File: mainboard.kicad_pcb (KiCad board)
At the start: 2 copper layers, 88 x 100 mm, 57 parts, among them J1 USB_C_Receptacle_USB2.0, J2 GPIO, J3 RJ45, J4 RJ45, J5 Conn_01x02_Socket, J6 Conn_01x03_Socket, M1 Fan, Q1 MMBT3904, Q2 MMBT3906, Q3 SSM3J332R, Q4 MMBT3906, SW1 SW_DIP_x02, U1 CH221K, U2 MCP251863, U3 NJM2845DL1, U4 MSP2807, U5 IM920c_ADP_IM920conn, Y1 4MHz

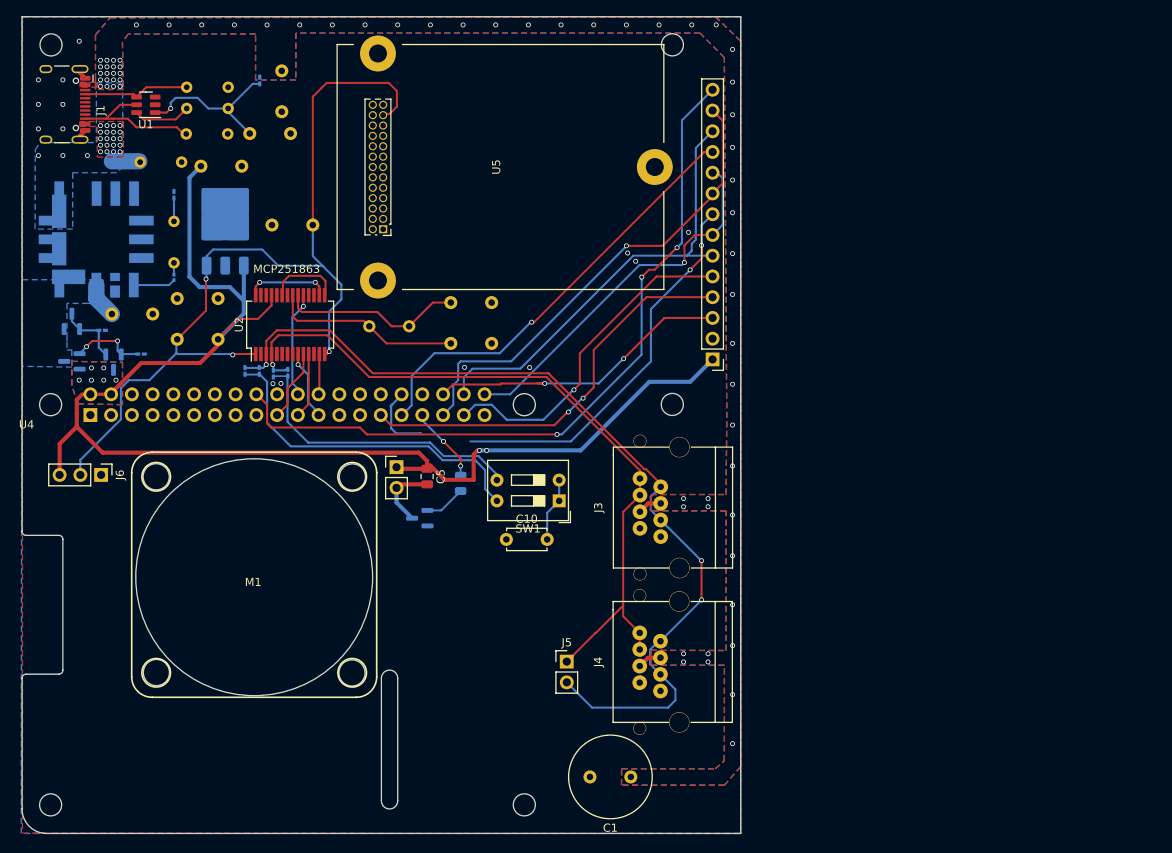
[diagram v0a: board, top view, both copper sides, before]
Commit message: チップ抵抗に変更
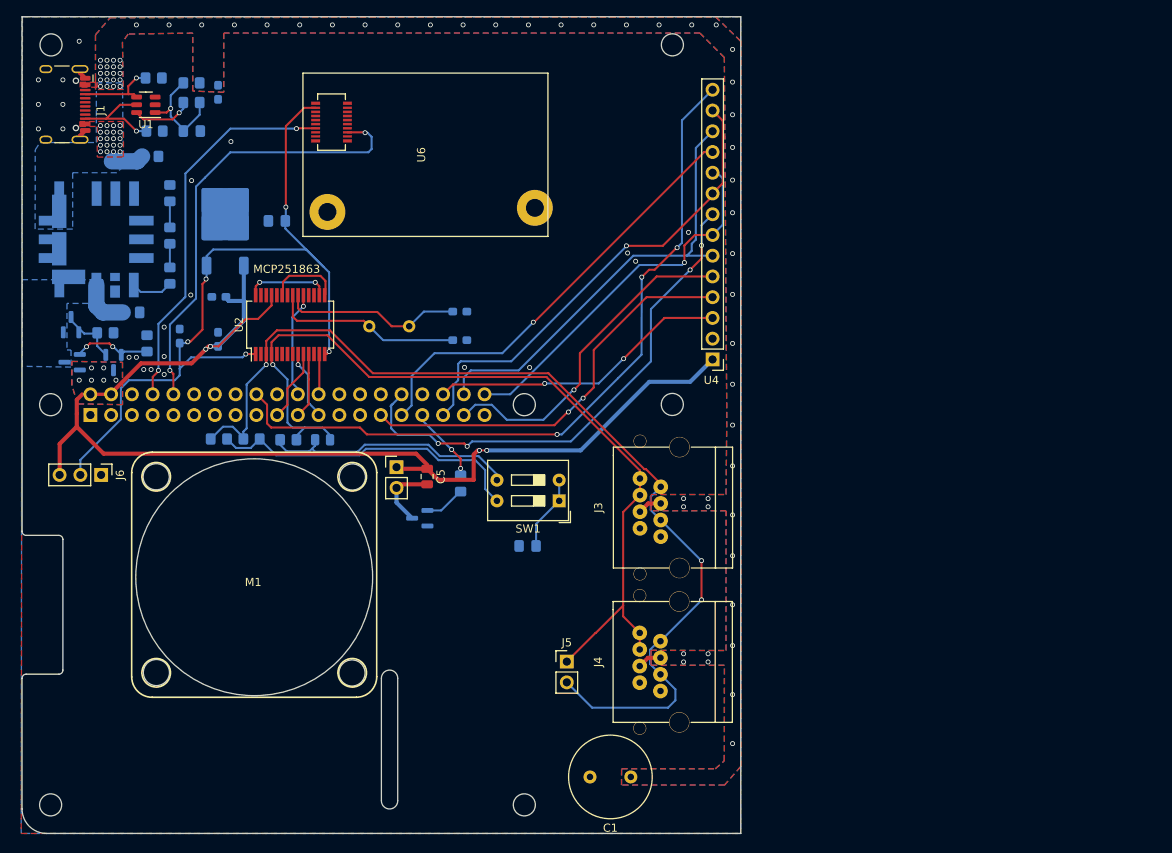
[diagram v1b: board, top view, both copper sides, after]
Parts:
- removed U5: IM920c_ADP_IM920conn, interplan:IM920(IM920c_ADP)
- added U6: IM920sl, interplan:IM920s, F.Cu at (157.5, 70.8)
- C10: footprint Capacitor_THT:C_Disc_D4.7mm_W2.5mm_P5.00mm -> Capacitor_SMD:C_0805_2012Metric_Pad1.18x1.45mm_HandSolder; moved to B.Cu
- C11: value 0.33μF -> 0.1μF; footprint Capacitor_THT:C_Disc_D4.7mm_W2.5mm_P5.00mm -> Capacitor_SMD:C_0603_1608Metric_Pad1.08x0.95mm_HandSolder
- C12: value 2.2µF -> 10µF; footprint Capacitor_THT:C_Disc_D4.7mm_W2.5mm_P5.00mm -> Capacitor_SMD:C_0805_2012Metric_Pad1.18x1.45mm_HandSolder
- C2, C4: footprint Capacitor_THT:C_Disc_D4.7mm_W2.5mm_P5.00mm -> Capacitor_SMD:C_0805_2012Metric_Pad1.18x1.45mm_HandSolder
- C3, C6, C7, C8, C9: footprint Capacitor_THT:C_Disc_D4.7mm_W2.5mm_P5.00mm -> Capacitor_SMD:C_0603_1608Metric_Pad1.08x0.95mm_HandSolder
- R1, R10, R11, R12, R13, R14, R9: footprint Resistor_SMD:R_0201_0603Metric_Pad0.64x0.40mm_HandSolder -> Resistor_SMD:R_0805_2012Metric_Pad1.20x1.40mm_HandSolder
- R15: footprint Resistor_SMD:R_0201_0603Metric_Pad0.64x0.40mm_HandSolder -> Resistor_SMD:R_0805_2012Metric
- R2, R3, R4, R5, R8: footprint Resistor_THT:R_Axial_DIN0204_L3.6mm_D1.6mm_P5.08mm_Horizontal -> Resistor_SMD:R_0805_2012Metric_Pad1.20x1.40mm_HandSolder
- R6: footprint Diode_SMD:D_0805_2012Metric -> Resistor_SMD:R_0805_2012Metric_Pad1.20x1.40mm_HandSolder
- R7: footprint Resistor_SMD:R_0201_0603Metric -> Resistor_SMD:R_0805_2012Metric_Pad1.20x1.40mm_HandSolder
- U3: value NJM2845DL1 -> NJM2391; footprint Package_TO_SOT_SMD:TO-252-3_TabPin2 -> Package_TO_SOT_SMD:TO-252-2
- moved C11 16.2 mm to (132.2, 88.2), turned to 180 degrees
- moved R15 9.24 mm to (144.9, 105.7), turned to 0 degrees
- moved R12 8.93 mm to (132.2, 105.5), turned to 180 degrees
- moved R13 8.39 mm to (136.2, 105.5), turned to 180 degrees
- moved R1 8.36 mm to (128.9, 62.0), turned to 180 degrees
- moved R14 8.30 mm to (140.8, 105.7), turned to 0 degrees
- moved C3 8.23 mm to (132.2, 63.1)
- moved C2 7.10 mm to (128.9, 67.8)
- moved R4 4.55 mm to (128.9, 64.3)
- moved C12 4.43 mm to (139.3, 78.8)
- moved R2 4.20 mm to (124.3, 61.4)
- moved C9 4.05 mm to (161.8, 90.0)
- moved C8 3.92 mm to (161.8, 93.5)
- moved R3 3.89 mm to (124.4, 67.8)
- moved R8 3.38 mm to (126.2, 80.7)
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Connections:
- J2 pad 10: /GPIO15/RXD0 -> UART RXD
- J2 pad 8: /GPIO14/TXD0 -> UART TXD
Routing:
- net UART RXD: track 0.00 -> 55.1 mm, vias 0 -> 2
- net UART TXD: track 0.00 -> 47.0 mm, vias 0 -> 2
- net +5V: track 165.6 -> 147.0 mm, vias 8 -> 10
- net /canfd/CANH: track 91.4 -> 105.0 mm
- net /canfd/CANL: track 111.1 -> 123.8 mm
- net +3.3V: track 109.5 -> 98.5 mm, vias 3 -> 5
- net Net-(U1-VDD): track 20.9 -> 13.3 mm
- net LED: track 56.3 -> 63.2 mm, vias 2 -> 4
- net Net-(J1-CC2): track 17.5 -> 12.2 mm, vias 0 -> 1
- net Net-(R14-Pad1): track 36.6 -> 31.6 mm
- net Net-(J1-CC1): track 13.1 -> 9.62 mm, vias 0 -> 1
- net Net-(R12-Pad1): track 41.5 -> 39.1 mm
- net Net-(P1-Sence): track 4.33 -> 6.10 mm
- net Net-(C10-Pad2): track 7.57 -> 9.24 mm
- net Net-(R7-Pad2): track 1.46 -> 2.90 mm
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
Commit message: first commit
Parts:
- removed ? (x3): , 
- removed C10: 4700pF, Capacitor_SMD:C_0805_2012Metric_Pad1.18x1.45mm_HandSolder
- removed C11: 0.1μF, Capacitor_SMD:C_0603_1608Metric_Pad1.08x0.95mm_HandSolder
- removed C12: 10µF, Capacitor_SMD:C_0805_2012Metric_Pad1.18x1.45mm_HandSolder
- removed M1: Fan, pihat_cooling:fan_30mm
- removed Q2, Q4: MMBT3906, Package_TO_SOT_SMD:SOT-23
- removed R10: 10KΩ, Resistor_SMD:R_0805_2012Metric_Pad1.20x1.40mm_HandSolder
- removed R12, R13, R14: 120Ω, Resistor_SMD:R_0805_2012Metric_Pad1.20x1.40mm_HandSolder
- removed R15: 120Ω, Resistor_SMD:R_0805_2012Metric
- removed S1, S2, S3, S4: M3, screw:M3
- removed SW1: SW_DIP_x02, Button_Switch_THT:SW_DIP_SPSTx02_Slide_9.78x7.26mm_W7.62mm_P2.54mm
- removed U6: IM920sl, interplan:IM920s
- removed Y1: 4MHz, Crystal:Crystal_HC49-U_Vertical
- added IC1: AZ1117CH-3.3TRG1, OKL:SOT230P700X180-4N, F.Cu at (130.2, 109.8)
- added J10: RJ45, OKL:7810-8P8C, F.Cu at (143.0, 145.0)
- added J11: Conn_01x02, Connector_JST:JST_XH_B2B-XH-A_1x02_P2.50mm_Vertical, F.Cu at (160.8, 150.8)
- added J13: Conn_01x04_Socket, Connector_JST:JST_XH_B4B-XH-A_1x04_P2.50mm_Vertical, F.Cu at (132.2, 133.1)
- added J2: Conn_01x03_Socket, Connector_PinHeader_2.54mm:PinHeader_1x03_P2.54mm_Vertical, F.Cu at (150.7, 110.1)
- added J7: Conn_01x04, Connector_JST:JST_XH_B4B-XH-A_1x04_P2.50mm_Vertical, F.Cu at (170.0, 136.0)
- added J8: Conn_01x02, Connector_JST:JST_XH_B2B-XH-A_1x02_P2.50mm_Vertical, F.Cu at (160.8, 142.9)
- added J9: RJ45, OKL:7810-8P8C, F.Cu at (123.0, 145.0)
- added X1: CSX-750P, OKL:CSX-750P, F.Cu at (144.4, 121.0)
- C1: value 1000μF -> 0.1μF; footprint Capacitor_THT:C_Radial_D10.0mm_H12.5mm_P5.00mm -> Capacitor_SMD:C_0603_1608Metric_Pad1.08x0.95mm_HandSolder
- C2: value 1μF -> 10µF; moved to F.Cu
- C3, C7: moved to F.Cu
- C4: value 10μF -> 0.1μF; footprint Capacitor_SMD:C_0805_2012Metric_Pad1.18x1.45mm_HandSolder -> Capacitor_SMD:C_0603_1608Metric_Pad1.08x0.95mm_HandSolder; moved to F.Cu
- C5: value 100nF -> 10μF; footprint Capacitor_SMD:C_0805_2012Metric -> Capacitor_SMD:C_0805_2012Metric_Pad1.18x1.45mm_HandSolder
- C6: value 0.1μF -> 100nF; footprint Capacitor_SMD:C_0603_1608Metric_Pad1.08x0.95mm_HandSolder -> Capacitor_SMD:C_0805_2012Metric; moved to F.Cu
- C8: value 22pF -> 0.1μF; moved to F.Cu
- C9: value 22pF -> 22μF; footprint Capacitor_SMD:C_0603_1608Metric_Pad1.08x0.95mm_HandSolder -> Capacitor_SMD:C_0805_2012Metric_Pad1.18x1.45mm_HandSolder; moved to F.Cu
- J1: value USB_C_Receptacle_USB2.0 -> Conn_01x04; footprint Connector_USB:USB_C_Receptacle_HCTL_HC-TYPE-C-16P-01A -> Connector_JST:JST_XH_B4B-XH-A_1x04_P2.50mm_Vertical
- J3: value RJ45 -> Conn_01x02_Socket; footprint akiRJ45:7810-8P8C -> Connector_PinHeader_2.54mm:PinHeader_1x02_P2.54mm_Vertical
- J4: value RJ45 -> Conn_01x04; footprint akiRJ45:7810-8P8C -> Connector_JST:JST_XH_B4B-XH-A_1x04_P2.50mm_Vertical
- J5: value Conn_01x02_Socket -> Conn_01x02; footprint Connector_PinHeader_2.54mm:PinHeader_1x02_P2.54mm_Vertical -> Connector_JST:JST_XH_B2B-XH-A_1x02_P2.50mm_Vertical
- J6: value Conn_01x03_Socket -> Conn_01x02; footprint Connector_PinHeader_2.54mm:PinHeader_1x03_P2.54mm_Vertical -> Connector_JST:JST_XH_B2B-XH-A_1x02_P2.50mm_Vertical
- P1: value ~ -> OKLT6W12NC; footprint okL:OKLT6W12NC -> OKL:OKLT6W12NC; moved to F.Cu
- Q1: value MMBT3904 -> IRFML8244TRPBF; footprint Package_TO_SOT_SMD:SOT-23 -> Package_TO_SOT_SMD:SOT-23-3; moved to F.Cu
- Q3: value SSM3J332R -> IRFML8244TRPBF; footprint Package_TO_SOT_SMD:SOT-23 -> Package_TO_SOT_SMD:SOT-23-3; moved to F.Cu
- R1: value 1kΩ -> 120Ω; moved to F.Cu
- R11: value 10KΩ -> R; footprint Resistor_SMD:R_0805_2012Metric_Pad1.20x1.40mm_HandSolder -> Resistor_SMD:R_0603_1608Metric_Pad0.98x0.95mm_HandSolder; moved to F.Cu
- R2: value 5.1kΩ -> 330Ω; moved to F.Cu
- R3: value 5.1kΩ -> 1kΩ; moved to F.Cu
- R4: value 47kΩ -> R; footprint Resistor_SMD:R_0805_2012Metric_Pad1.20x1.40mm_HandSolder -> Resistor_SMD:R_0603_1608Metric_Pad0.98x0.95mm_HandSolder; moved to F.Cu
- R5: value 20KΩ -> 10Ω; moved to F.Cu
- R6: value 100 -> R; footprint Resistor_SMD:R_0805_2012Metric_Pad1.20x1.40mm_HandSolder -> Resistor_SMD:R_0603_1608Metric_Pad0.98x0.95mm_HandSolder
- R7: value 1kΩ -> R; footprint Resistor_SMD:R_0805_2012Metric_Pad1.20x1.40mm_HandSolder -> Resistor_SMD:R_0603_1608Metric_Pad0.98x0.95mm_HandSolder
- R8: value 330Ω -> R; footprint Resistor_SMD:R_0805_2012Metric_Pad1.20x1.40mm_HandSolder -> Resistor_SMD:R_0603_1608Metric_Pad0.98x0.95mm_HandSolder
- R9: value 10Ω -> R; footprint Resistor_SMD:R_0805_2012Metric_Pad1.20x1.40mm_HandSolder -> Resistor_SMD:R_0603_1608Metric_Pad0.98x0.95mm_HandSolder; moved to F.Cu
- U1: value CH221K -> MCP251863; footprint Package_TO_SOT_SMD:SOT-23-6 -> Package_SO:SSOP-28_5.3x10.2mm_P0.65mm
- U2: value MCP251863 -> TCA9803; footprint Package_SO:SSOP-28_5.3x10.2mm_P0.65mm -> Package_SO:VSSOP-8_3.0x3.0mm_P0.65mm
- U3: value NJM2391 -> TCA9803; footprint Package_TO_SOT_SMD:TO-252-2 -> Package_SO:VSSOP-8_3.0x3.0mm_P0.65mm; moved to F.Cu
- U4: value MSP2807 -> TCA9803; footprint MSP2807:MSP2807 -> Package_SO:VSSOP-8_3.0x3.0mm_P0.65mm
- moved R8 75.3 mm to (155.4, 150.1), turned to -90 degrees
- moved J1 72.3 mm to (170.0, 108.0)
- moved R7 63.8 mm to (155.2, 142.4)
- moved C9 62.4 mm to (119.5, 135.8), turned to 0 degrees
- moved R4 60.1 mm to (153.8, 119.0)
- moved R1 57.6 mm to (154.7, 113.4), turned to 0 degrees
- moved P1 57.0 mm to (114.8, 131.8), turned to 90 degrees
- moved C3 55.9 mm to (161.6, 110.6), turned to 0 degrees
- moved R2 55.6 mm to (131.5, 116.5)
- moved U3 55.2 mm to (162.5, 126.0), turned to 0 degrees
- moved R9 52.4 mm to (131.4, 127.6)
- moved C1 52.1 mm to (149.6, 106.6), turned to 0 degrees
- moved U1 50.7 mm to (142.4, 111.6), turned to -90 degrees
- moved R5 49.7 mm to (132.6, 119.9), turned to -90 degrees
- moved R3 48.8 mm to (127.0, 116.6)
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- renumbered J2 to J12
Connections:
- net D/C renamed EN_3
- C1 pad 1: +12V -> +3.3V
- C2 pad 1: Net-(U1-VDD) -> +3.3V
- C3 pad 1: +12V -> +3.3V
- C4 pad 1: Net-(P1-Sence) -> +5V
- C5 pad 2: Net-(M1--) -> GND
- C7 pad 1: +5V -> +3.3V
- C8 pad 1: GND -> +3.3V
- C8 pad 2: Net-(U2-OSC1) -> GND
- C9 pad 1: GND -> +12V
- C9 pad 2: Net-(U2-OSC2) -> GND
- J12 pad 11: /GPIO17 -> LED_B
- J12 pad 13: /GPIO27 -> LED_R
- J12 pad 32: LED -> limit1
- J12 pad 33: GPIO13/PWM1 -> EN_1
- J12 pad 35: SPI1.MISO -> EN_2
- J12 pad 36: SPI1.CE0 -> limit2
- J12 pad 38: SPI1.MOSI -> limit3
- J12 pad 40: SPI1.SCLK -> limit4
- J3 pad 1: /canfd/CANH -> Net-(J3-Pin_1)
- J3 pad 2: /canfd/CANL -> /canfd/CANH
- J4 pad 1: /canfd/CANH -> Net-(J4-Pin_1)
- J4 pad 2: /canfd/CANL -> Net-(J4-Pin_2)
- J4 pad 3: /canfd/CANH -> +3.3V
- J4 pad 4: +12V -> GND
- J5 pad 1: /canfd/CANH -> +3.3V
- J5 pad 2: /canfd/CANL -> limit1
- J6 pad 1: GND -> +3.3V
- J6 pad 2: +3.3V -> limit2
- P1 pad 4: Net-(P1-Sence) -> +5V
- P1 pad 5: Net-(P1-Sence) -> +5V
- Q1 pad 1: Net-(Q1-B) -> LED_B
- Q1 pad 3: Net-(M1--) -> Net-(J13-Pin_2)
- Q3 pad 1: Net-(Q3-G) -> LED_R
- Q3 pad 2: +5V -> GND
- Q3 pad 3: Net-(P1-Sence) -> Net-(J13-Pin_4)
- R1 pad 1: +12V -> Net-(J3-Pin_1)
- R1 pad 2: Net-(U1-VDD) -> /canfd/CANL
- R11 pad 1: Net-(Q3-G) -> GND
- R11 pad 2: GND -> LED_R
- R2 pad 1: Net-(J1-CC1) -> Net-(R2-Pad1)
- R2 pad 2: GND -> Net-(R2-Pad2)
- R3 pad 1: Net-(J1-CC2) -> Net-(P1-Trim)
- R3 pad 2: GND -> Net-(R2-Pad1)
- R4 pad 1: Net-(U1-VDD) -> limit1
- R4 pad 2: Net-(U1-CFG) -> GND
- R5 pad 1: +12V -> Net-(R2-Pad2)
- R6 pad 1: Net-(Q1-B) -> limit2
- R6 pad 2: GPIO13/PWM1 -> GND
- R7 pad 1: Net-(P1-Trim) -> limit3
- R7 pad 2: Net-(R7-Pad2) -> GND
- R8 pad 1: Net-(R7-Pad2) -> limit4
- R8 pad 2: Net-(R8-Pad2) -> GND
- R9 pad 1: Net-(R8-Pad2) -> GND
- R9 pad 2: GND -> LED_B
- U1 pad 1: Net-(U1-VDD) -> +3.3V
- U1 pad 2: GND -> unconnected-(U1-NC-Pad2)
- U1 pad 3: unconnected-(U1-PG-Pad3) -> /canfd/CANL
- U1 pad 4: Net-(J1-CC1) -> /canfd/CANH
- U1 pad 5: Net-(J1-CC2) -> GND
- U1 pad 6: Net-(U1-CFG) -> unconnected-(U1-nINT1-Pad6)
- U2 pad 2: unconnected-(U2-NC-Pad2) -> /GPIO3/SCL1
- U2 pad 3: /canfd/CANL -> /GPIO2/SDA1
- U2 pad 4: /canfd/CANH -> GND
- U2 pad 5: GND -> EN_1
- U2 pad 6: unconnected-(U2-nINT1-Pad6) -> Net-(J1-Pin_2)
- U2 pad 7: unconnected-(U2-nINT0-Pad7) -> Net-(J1-Pin_1)
- U2 pad 8: unconnected-(U2-NC-Pad8) -> +3.3V
- U3 pad 1: +5V -> +3.3V
- U3 pad 2: GND -> /GPIO3/SCL1
- U3 pad 3: +3.3V -> /GPIO2/SDA1
- U4 pad 1: +5V -> +3.3V
- U4 pad 2: GND -> /GPIO3/SCL1
- U4 pad 3: SPI1.CE0 -> /GPIO2/SDA1
- U4 pad 4: RESET -> GND
- U4 pad 6: SPI1.MOSI -> Net-(J7-Pin_2)
- U4 pad 7: SPI1.SCLK -> Net-(J7-Pin_1)
- U4 pad 8: LED -> +3.3V
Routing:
- net +3.3V: track 98.5 -> 198.8 mm, vias 5 -> 4
- net IRQ: track 91.4 -> 0.00 mm, vias 3 -> 0
- net +5V: track 147.0 -> 66.8 mm, vias 10 -> 2
- net /GPIO3/SCL1: track 0.00 -> 79.5 mm, vias 0 -> 3
- net /GPIO2/SDA1: track 0.00 -> 79.4 mm, vias 0 -> 1
- net limit4: track 0.00 -> 73.3 mm
- net LED: track 63.2 -> 0.00 mm, vias 4 -> 0
- net SPI1.MISO: track 58.4 -> 0.00 mm, vias 1 -> 0
- net SPI1.MOSI: track 55.2 -> 0.00 mm
- net UART RXD: track 55.1 -> 0.00 mm, vias 2 -> 0
- net limit3: track 0.00 -> 54.2 mm
- net SPI1.CE1: track 53.5 -> 0.06 mm, vias 1 -> 0
- net RESET: track 50.7 -> 0.00 mm, vias 2 -> 0
- net limit2: track 0.00 -> 49.4 mm, vias 0 -> 1
- net UART TXD: track 47.0 -> 0.00 mm, vias 2 -> 0
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- removed copper zone on B.Cu, net +12V
- removed copper zone on F.Cu, net +12V
- removed copper zone on B.Cu, net +5V
- removed copper zone on F.Cu, net +5V
- removed copper zone on B.Cu, net Net-(P1-Sence)
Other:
- board size 88 x 100 mm -> 65 x 56 mm
- board text added: "サレジオ高専 ロボコンプロジェクト 制御班2024"
- board text removed: "PoE"

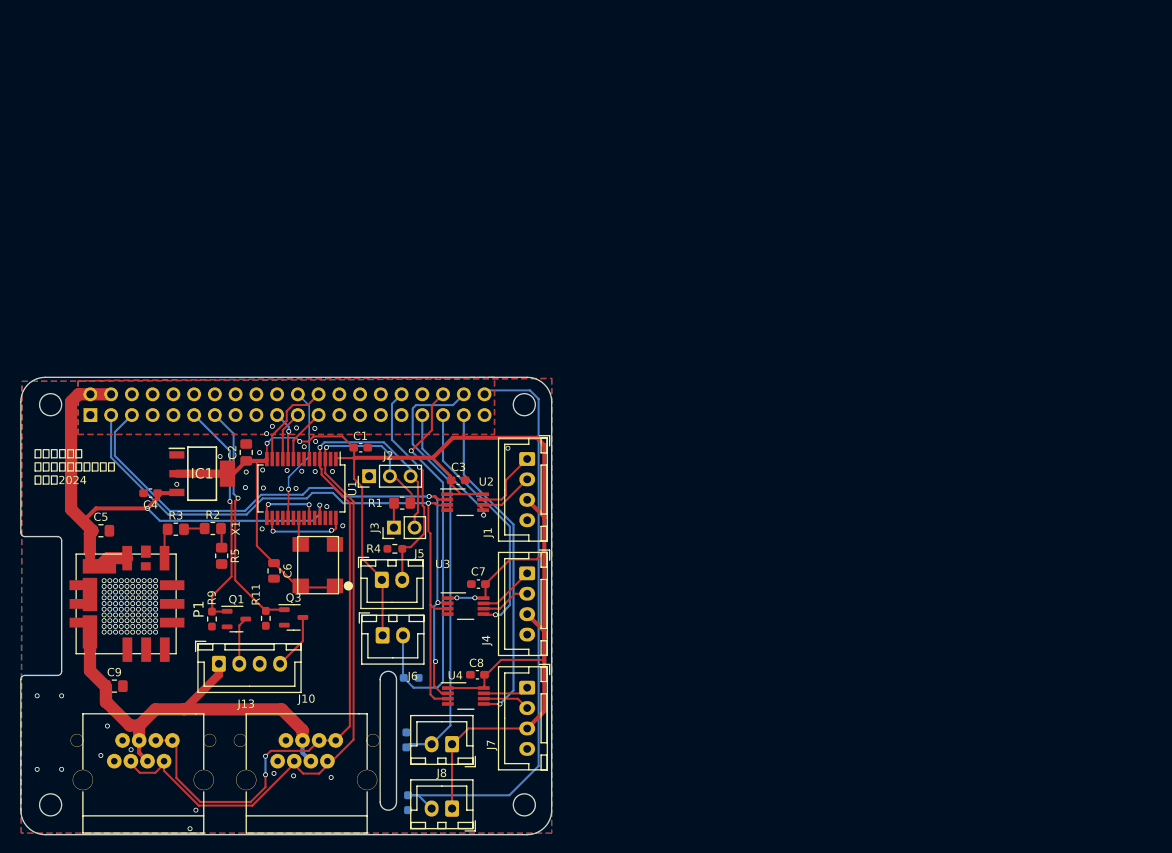
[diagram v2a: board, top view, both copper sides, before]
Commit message: 2chに変更
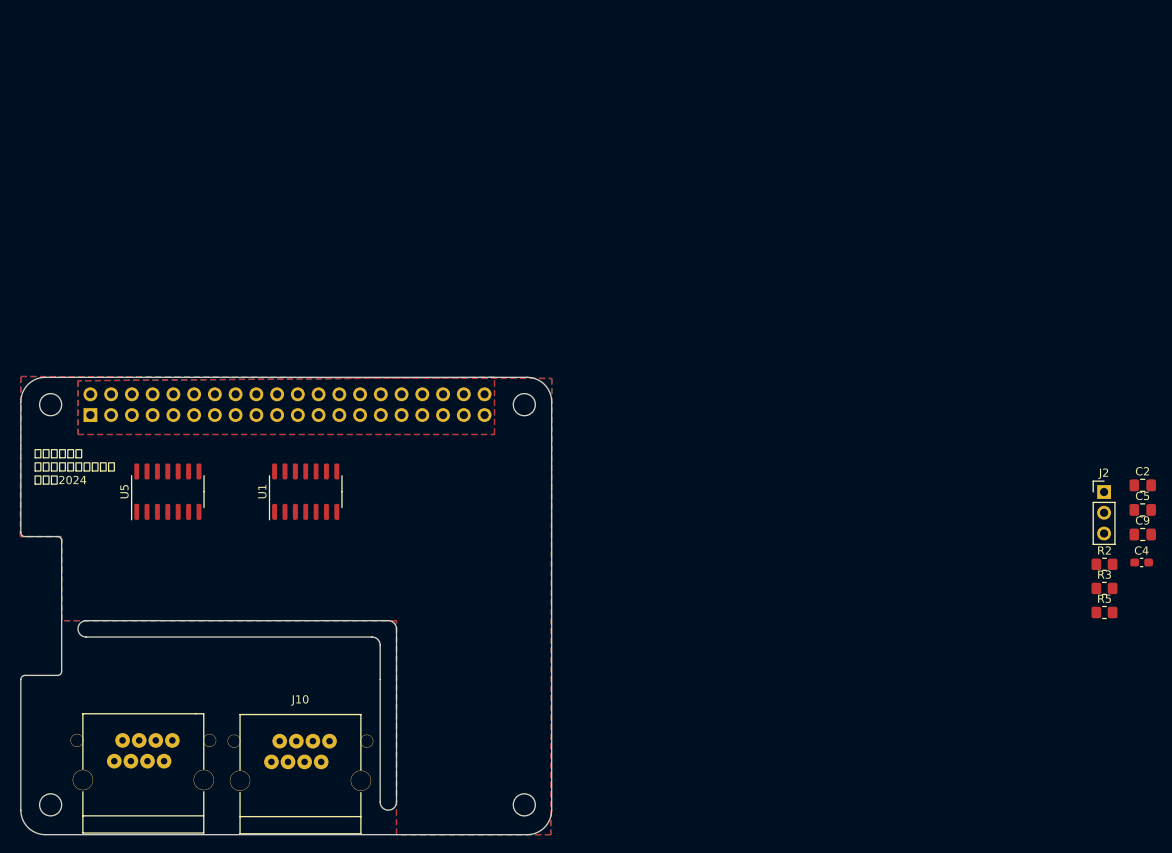
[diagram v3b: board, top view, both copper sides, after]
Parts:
- removed C1, C3, C7, C8: 0.1μF, Capacitor_SMD:C_0603_1608Metric_Pad1.08x0.95mm_HandSolder
- removed C6: 100nF, Capacitor_SMD:C_0805_2012Metric
- removed IC1: AZ1117CH-3.3TRG1, OKL:SOT230P700X180-4N
- removed J1, J4, J7: Conn_01x04, Connector_JST:JST_XH_B4B-XH-A_1x04_P2.50mm_Vertical
- removed J11, J5, J6, J8: Conn_01x02, Connector_JST:JST_XH_B2B-XH-A_1x02_P2.50mm_Vertical
- removed J13: Conn_01x04_Socket, Connector_JST:JST_XH_B4B-XH-A_1x04_P2.50mm_Vertical
- removed J3: Conn_01x02_Socket, Connector_PinHeader_2.54mm:PinHeader_1x02_P2.54mm_Vertical
- removed P1: OKLT6W12NC, OKL:OKLT6W12NC
- removed Q1, Q3: IRFML8244TRPBF, Package_TO_SOT_SMD:SOT-23-3
- removed R1: 120Ω, Resistor_SMD:R_0805_2012Metric_Pad1.20x1.40mm_HandSolder
- removed R11, R4, R6, R7, R8, R9: R, Resistor_SMD:R_0603_1608Metric_Pad0.98x0.95mm_HandSolder
- removed U2, U3, U4: TCA9803, Package_SO:VSSOP-8_3.0x3.0mm_P0.65mm
- removed X1: CSX-750P, OKL:CSX-750P
- added U5: MCP2517FD-xSL, Package_SO:SOIC-14_3.9x8.7mm_P1.27mm, F.Cu at (126.0, 112.0)
- U1: value MCP251863 -> MCP2517FD-xSL; footprint Package_SO:SSOP-28_5.3x10.2mm_P0.65mm -> Package_SO:SOIC-14_3.9x8.7mm_P1.27mm
- moved C5 127.6 mm to (245.4, 114.2)
- moved C9 127.3 mm to (245.4, 117.2)
- moved C4 121.6 mm to (245.2, 120.7), turned to 0 degrees
- moved R3 113.9 mm to (240.7, 123.8)
- moved C2 109.8 mm to (245.4, 111.2), turned to 0 degrees
- moved R2 109.3 mm to (240.7, 120.9)
- moved R5 108.3 mm to (240.7, 126.8), turned to 0 degrees
- moved J2 90.0 mm to (240.6, 112.0), turned to 0 degrees
- moved J10 0.77 mm to (142.2, 145.1)
- moved U1 0.66 mm to (142.9, 112.0), turned to 90 degrees
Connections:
- J10 pad 1: /canfd/CANH -> Net-(J2-Pin_3)
- J10 pad 2: /canfd/CANL -> Net-(J2-Pin_2)
- J10 pad 3: /canfd/CANH -> Net-(J2-Pin_3)
- J10 pad 6: /canfd/CANL -> Net-(J2-Pin_2)
- J2 pad 2: /canfd/CANL -> Net-(J2-Pin_2)
- J2 pad 3: /canfd/CANH -> Net-(J2-Pin_3)
- J9 pad 1: /canfd/CANH -> Net-(J2-Pin_3)
- J9 pad 2: /canfd/CANL -> Net-(J2-Pin_2)
- J9 pad 3: /canfd/CANH -> Net-(J2-Pin_3)
- J9 pad 6: /canfd/CANL -> Net-(J2-Pin_2)
- U1 pad 1: +3.3V -> unconnected-(U1-TXCAN-Pad1)
- U1 pad 10: SPI0.MOSI -> unconnected-(U1-SCK-Pad10)
- U1 pad 11: SPI0.MISO -> unconnected-(U1-SDI-Pad11)
- U1 pad 13: SPI0.CE0 -> unconnected-(U1-nCS-Pad13)
- U1 pad 14: +3.3V -> unconnected-(U1-VDD-Pad14)
- U1 pad 3: /canfd/CANL -> unconnected-(U1-CLKO/SOF-Pad3)
- U1 pad 4: /canfd/CANH -> unconnected-(U1-~{INT}-Pad4)
- U1 pad 5: GND -> unconnected-(U1-OSC2-Pad5)
- U1 pad 9: SPI0.SCLK -> unconnected-(U1-~{INT0}/GPIO0/XSTBY-Pad9)
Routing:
- net +3.3V: track 198.8 -> 0.00 mm, vias 4 -> 0
- net /canfd/CANH: track 92.0 -> 0.00 mm, vias 3 -> 0
- net /canfd/CANL: track 90.2 -> 0.00 mm, vias 1 -> 0
- net /GPIO3/SCL1: track 79.5 -> 0.00 mm, vias 3 -> 0
- net /GPIO2/SDA1: track 79.4 -> 0.00 mm, vias 1 -> 0
- net limit4: track 73.3 -> 0.00 mm
- net +5V: track 66.8 -> 0.00 mm, vias 2 -> 0
- net limit3: track 54.2 -> 0.00 mm
- net +12V: track 52.9 -> 0.00 mm
- net limit2: track 49.4 -> 0.00 mm, vias 1 -> 0
- net EN_3: track 40.9 -> 0.00 mm, vias 1 -> 0
- net EN_2: track 30.5 -> 0.00 mm, vias 1 -> 0
- net LED_R: track 29.2 -> 0.00 mm, vias 1 -> 0
- net LED_B: track 29.0 -> 0.00 mm, vias 1 -> 0
- net limit1: track 26.4 -> 0.00 mm, vias 1 -> 0
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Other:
- outline, holes or cut-outs redrawn

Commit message: 更新
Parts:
- added U2: MCP2562-E-SN, Package_SO:SOIC-8_3.9x4.9mm_P1.27mm, F.Cu at (119.0, 134.2)
- added U3: MCP2562-E-SN, Package_SO:SOIC-8_3.9x4.9mm_P1.27mm, F.Cu at (137.2, 134.1)
- moved C2 83.0 mm to (162.7, 118.4)
- moved C5 83.0 mm to (162.7, 121.4)
- moved C9 83.0 mm to (162.7, 124.4)
- moved J2 83.0 mm to (158.0, 119.2)
- moved C4 78.2 mm to (167.3, 127.0)
- moved R2 73.2 mm to (167.5, 118.4)
- moved R3 73.2 mm to (167.5, 121.3)
- moved R5 73.2 mm to (167.5, 124.3)
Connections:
- U5 pad 10: unconnected-(U5-SCK-Pad10) -> SPI0.SCLK
- U5 pad 11: unconnected-(U5-SDI-Pad11) -> SPI0.MOSI
- U5 pad 12: unconnected-(U5-SDO-Pad12) -> SPI0.MISO
- U5 pad 13: unconnected-(U5-nCS-Pad13) -> SPI0.CE0
- U5 pad 4: unconnected-(U5-~{INT}-Pad4) -> INT
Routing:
- added copper zone on B.Cu, net +3.3V
- added copper zone on F.Cu, net +3.3V
